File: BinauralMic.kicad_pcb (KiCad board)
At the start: 4 copper layers, 45 x 34.2 mm, 69 parts, among them IC1 PCM2903CDBR, J2 USB4105-GF-A-120, J3 Conn_01x02_Pin, J4 Conn_01x02_Pin, U1 MIC5504-3.3YM5, U2 TL972QDRQ1, U3 74LVC1G08, Y1 ABLS-12.000MHZ-20-D-3-H-T

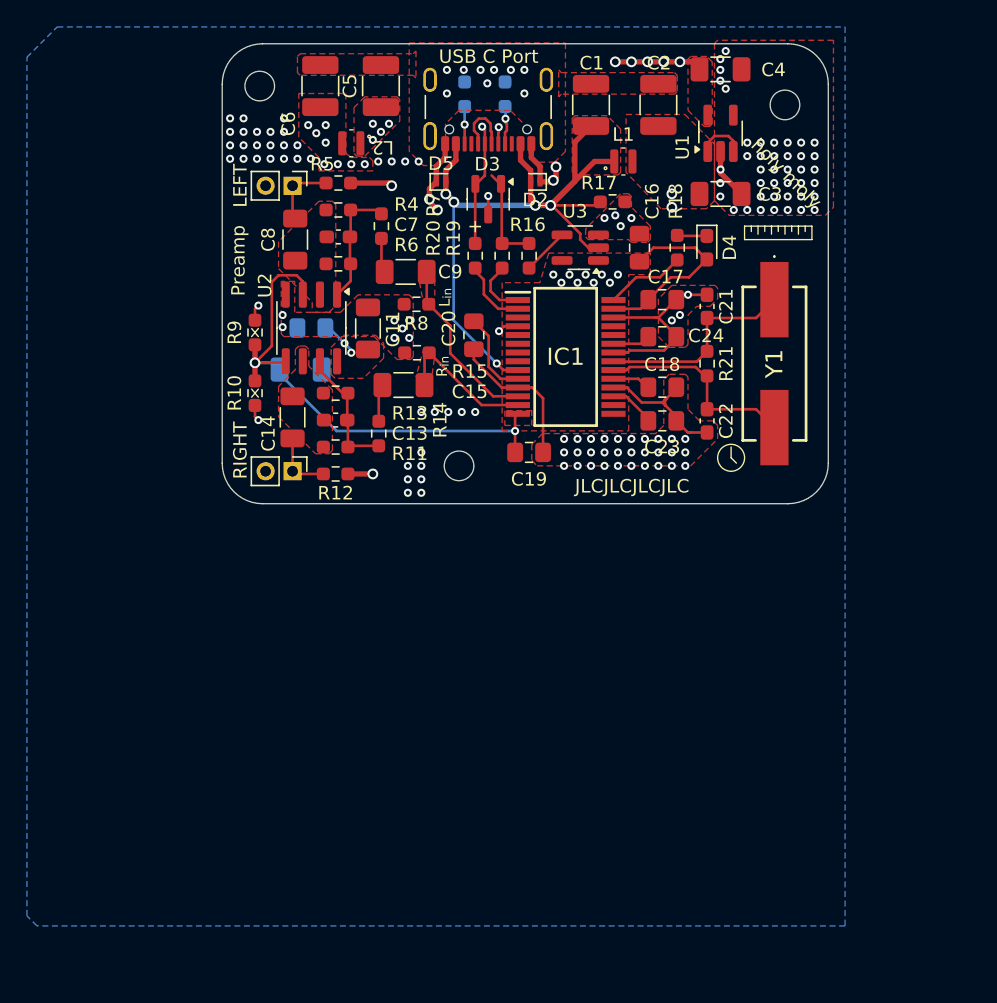
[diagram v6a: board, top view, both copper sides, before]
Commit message: Redid schematic and component values according to new recalculations
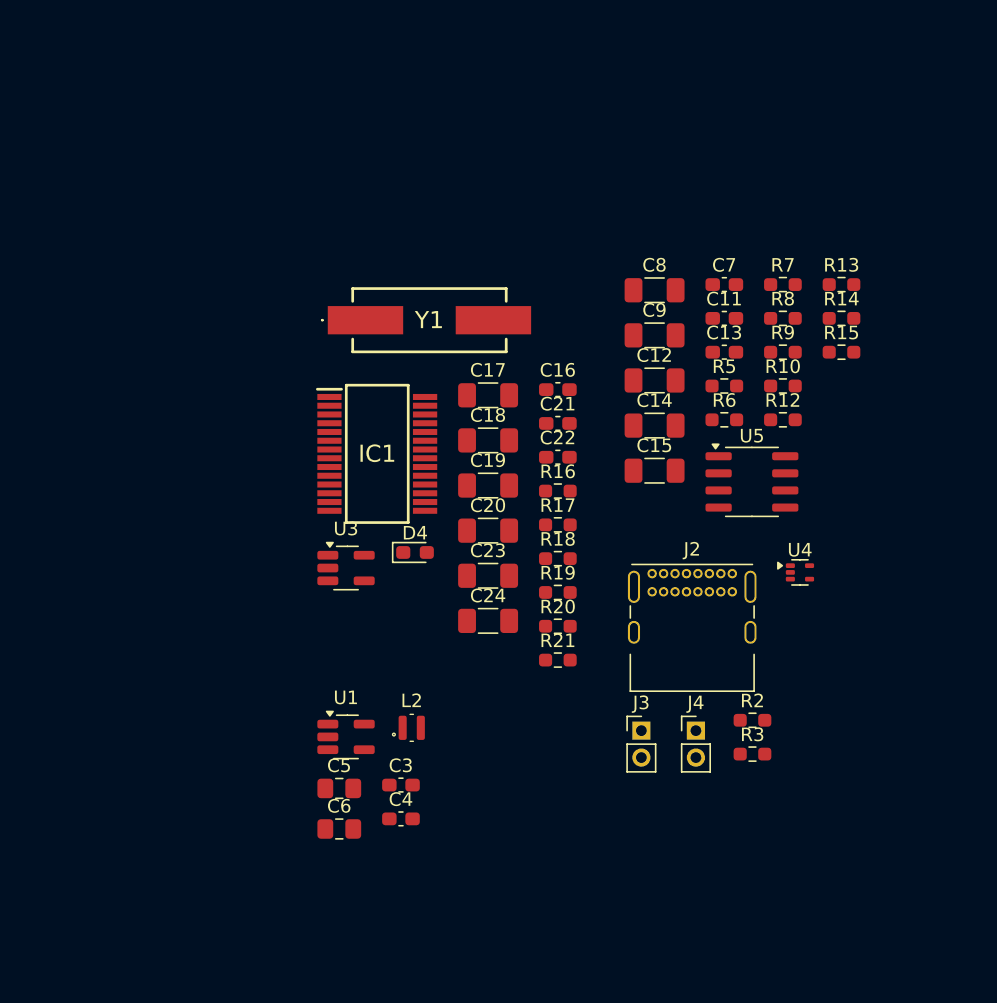
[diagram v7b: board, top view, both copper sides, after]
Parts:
- removed C1, C2: 22u, Capacitor_SMD:C_1210_3225Metric_Pad1.33x2.70mm_HandSolder
- removed C10: 0.1u, Capacitor_SMD:C_0805_2012Metric_Pad1.18x1.45mm_HandSolder
- removed D2, D5: PESD5V5C1BL, Diode_SMD:D_SOD-882
- removed D3: PESD2USB3UVT-QR, Package_TO_SOT_SMD:SOT-23-3
- removed G*** (x8): LOGO, LOGO
- removed L1: XFL2010-823ME, Inductor_SMD:L_Coilcraft_XFL2010
- removed R11, R4: 1M, Resistor_SMD:R_0603_1608Metric_Pad0.98x0.95mm_HandSolder
- removed REF** (x3): MountingHole_2.2mm_M2, MountingHole:MountingHole_2.2mm_M2
- removed U2: TL972QDRQ1, Package_SO:SOIC-8_3.9x4.9mm_P1.27mm
- added U4: TPD3E001DRLR, Package_TO_SOT_SMD:SOT-553, F.Cu at (163.7, 90.3)
- added U5: MC33078, Package_SO:SOIC-8_3.9x4.9mm_P1.27mm, F.Cu at (160.1, 83.6)
- C11, C3, C4: footprint Capacitor_SMD:C_1206_3216Metric_Pad1.33x1.80mm_HandSolder -> Capacitor_SMD:C_0603_1608Metric_Pad1.08x0.95mm_HandSolder
- C12: value 4.7u -> 10u; moved to F.Cu
- C13, C7: value 68p -> 47p
- C14, C15, C8, C9: value 4.7u -> 10u
- C16: footprint Capacitor_SMD:C_0805_2012Metric_Pad1.18x1.45mm_HandSolder -> Capacitor_SMD:C_0603_1608Metric_Pad1.08x0.95mm_HandSolder
- C17, C18, C19, C20, C23, C24: footprint Capacitor_SMD:C_0805_2012Metric_Pad1.18x1.45mm_HandSolder -> Capacitor_SMD:C_1206_3216Metric_Pad1.33x1.80mm_HandSolder
- C21, C22: value 16p -> 36p
- C5, C6: footprint Capacitor_SMD:C_1210_3225Metric_Pad1.33x2.70mm_HandSolder -> Capacitor_SMD:C_0805_2012Metric_Pad1.18x1.45mm_HandSolder
- J2: footprint Connector_USB:USB_C_Receptacle_GCT_USB4105-xx-A_16P_TopMnt_Horizontal -> Connector_USB:USB_C_Receptacle_GCT_USB4085
- R10: value 100k -> 200k
- R13, R6: value 18k -> 24k
- R18: value 5.6k -> 1k
- R2, R3: moved to F.Cu
- moved C4 60.5 mm to (134.1, 108.6)
- moved C6 55.2 mm to (129.5, 109.4), turned to 0 degrees
- moved R3 53.4 mm to (160.2, 103.8), turned to 0 degrees
- moved U1 52.7 mm to (130.0, 102.5), turned to 0 degrees
- moved C5 52.2 mm to (129.5, 106.3), turned to 0 degrees
- moved J4 50.3 mm to (156.0, 102.1), turned to 0 degrees
- moved R2 50.0 mm to (160.2, 101.3), turned to 0 degrees
- moved C3 49.9 mm to (134.1, 106.1)
- moved L2 43.6 mm to (134.9, 101.8), turned to 0 degrees
- moved R9 39.2 mm to (162.4, 74.0), turned to 0 degrees
- moved R10 39.2 mm to (162.4, 76.5), turned to 0 degrees
- moved R13 38.4 mm to (166.8, 68.9)
- moved J2 37.6 mm to (152.7, 90.4), turned to 0 degrees
- moved R14 35.4 mm to (166.8, 71.5), turned to 0 degrees
- moved R12 33.5 mm to (162.4, 79.0), turned to 0 degrees
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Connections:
- C11 pad 1: +3.3VA -> +5VA
- C3 pad 1: +5V -> /VBUS
- C5 pad 1: VCC -> /VBUS
- C6 pad 1: +3.3VA -> +5VA
- L2 pad 1: VCC -> /VBUS
- L2 pad 2: +3.3VA -> +5VA
- R12 pad 1: +5V -> +5VA
- R5 pad 1: +5V -> +5VA
- R9 pad 1: +3.3VA -> +5VA
- U1 pad 1: +5V -> /VBUS
- U1 pad 3: +5V -> /VBUS
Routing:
- net /VCOM: track 62.8 -> 0.00 mm, vias 2 -> 0
- net +5V: track 62.6 -> 0.00 mm, vias 4 -> 0
- net /VBUS: track 56.7 -> 0.00 mm, vias 5 -> 0
- net GND: track 55.2 -> 0.00 mm, vias 139 -> 0
- net VCC: track 36.3 -> 0.00 mm, vias 18 -> 0
- net /USB ADC/XTO: track 15.3 -> 0.00 mm
- net /USB ADC/XTI: track 15.3 -> 0.00 mm
- net /VIN_{L}: track 13.1 -> 0.00 mm
- net /D+: track 12.1 -> 0.00 mm
- net /D-: track 11.6 -> 0.00 mm, vias 2 -> 0
- net /VIN_{R}: track 10.7 -> 0.00 mm
- net /Mic Preamp/VOUT_{R}: track 9.82 -> 0.00 mm
- net /Mic Preamp/VOUT_{L}: track 9.15 -> 0.00 mm
- net /USB ADC/~{SSPND}: track 5.97 -> 0.00 mm
- net /USB ADC/D_R-: track 5.11 -> 0.00 mm
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- removed copper zone on F.Cu, net +3.3VA
- removed copper zone on In2.Cu, net +3.3VA
- removed copper zone on F.Cu, net +5V
- removed copper zone on F.Cu, net /Mic Preamp/VN_{L}
- removed copper zone on F.Cu, net /Mic Preamp/VN_{R}
- removed copper zone on F.Cu, net /VBUS
- removed copper zone on F.Cu, net /VCOM
- removed copper zone on F.Cu, net /VIN_{L}
- removed copper zone on F.Cu, net /VIN_{R}
- removed copper zone on B.Cu, net GND
- removed copper zone on F.Cu, net GND
- removed copper zone on In1.Cu, net GND
- removed copper zone on In2.Cu, net GND
- removed copper zone on F.Cu, net VCC
- removed copper zone on In2.Cu, net VCC
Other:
- board outline removed
- copper layers 4 -> 2
- board text removed: "+"
- board text removed: "BINAURAL MICROPHONE"
- board text removed: "Based on the PCM2903C"
- board text removed: "Besties"
- board text removed: "Contact @leftisttachyon for support"
- board text removed: "JJJJJJJJ"
- board text removed: "JLCJLCJLCJLC"
- board text removed: "LEFT"
- board text removed: "L_{in}"
- board text removed: "LeftistTachyon, 2024"
- board text removed: "Preamp"
- board text removed: "RIGHT"
- board text removed: "R_{in}"
- board text removed: "Source: @unenemiko"
- board text removed: "Special thanks to: MorrisYLin for reviewing the board Noccant for the funding"
- board text removed: "USB C Port"
- board text removed: "^{+}LEFT^{-}"
- board text removed: "_{+}RIGHT_{-}"
- board text removed: "holy moly"
- board text removed: "https://github.com/ LeftistTachyon/BinauralMic"
- board text removed: "the"
- board text removed: "凹凸"

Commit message: Add buttons for device control + various other changes
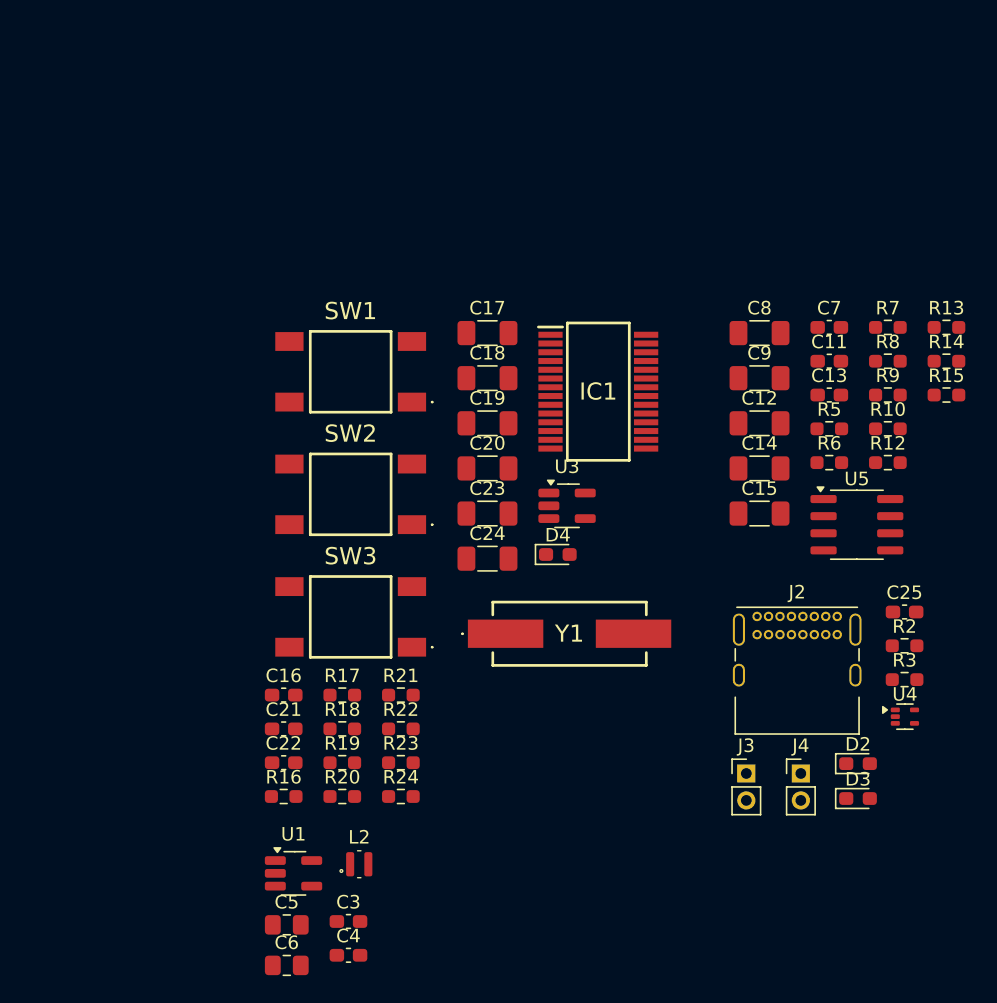
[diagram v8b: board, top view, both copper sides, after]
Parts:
- added C25: 0.1u, Capacitor_SMD:C_0603_1608Metric_Pad1.08x0.95mm_HandSolder, F.Cu at (171.5, 93.2)
- added D2: PESD5V0X1BCSF, Diode_SMD:D_0603_1608Metric_Pad1.05x0.95mm_HandSolder, F.Cu at (168.0, 104.5)
- added D3: PESD5V0X1BCSF, Diode_SMD:D_0603_1608Metric_Pad1.05x0.95mm_HandSolder, F.Cu at (168.0, 107.1)
- added R22: 1.5k, Resistor_SMD:R_0603_1608Metric_Pad0.98x0.95mm_HandSolder, F.Cu at (134.1, 101.9)
- added R23: 1.5k, Resistor_SMD:R_0603_1608Metric_Pad0.98x0.95mm_HandSolder, F.Cu at (134.1, 104.4)
- added R24: 1.5k, Resistor_SMD:R_0603_1608Metric_Pad0.98x0.95mm_HandSolder, F.Cu at (134.1, 107.0)
- added SW1: 2-1977223-4, binauralmic:219772234, F.Cu at (130.4, 75.4)
- added SW2: 2-1977223-4, binauralmic:219772234, F.Cu at (130.4, 84.5)
- added SW3: 2-1977223-4, binauralmic:219772234, F.Cu at (130.4, 93.6)
- moved C16 30.5 mm to (125.4, 99.4)
- moved C21 30.5 mm to (125.4, 101.9)
- moved R16 30.5 mm to (125.4, 107.0)
- moved C22 30.5 mm to (125.4, 104.4)
- moved Y1 25.5 mm to (146.6, 94.9)
- moved R17 20.4 mm to (129.7, 99.4)
- moved R18 20.4 mm to (129.7, 101.9)
- moved R19 20.4 mm to (129.7, 104.4)
- moved R20 20.4 mm to (129.7, 107.0)
- moved IC1 17.1 mm to (148.7, 76.9)
- moved U3 17.1 mm to (146.4, 85.4)
- moved U4 13.2 mm to (171.5, 101.0)
- moved R2 12.6 mm to (171.5, 95.8)
- moved R3 12.6 mm to (171.5, 98.3)
- moved R21 11.9 mm to (134.1, 99.4)
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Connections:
- IC1 pad 5: unconnected-(IC1-HID0-Pad5) -> /USB ADC/HID0
- IC1 pad 6: unconnected-(IC1-HID1-Pad6) -> /USB ADC/HID1
- IC1 pad 7: unconnected-(IC1-HID2-Pad7) -> /USB ADC/HID2
- J3 pad 2: /VCOM -> GND
- J4 pad 2: /VCOM -> GND
- R10 pad 1: /VCOM -> +5VA
- R10 pad 2: GND -> /VCOM
- R9 pad 1: +5VA -> /VCOM
- R9 pad 2: /VCOM -> GND
